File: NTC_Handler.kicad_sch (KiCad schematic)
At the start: 47 parts

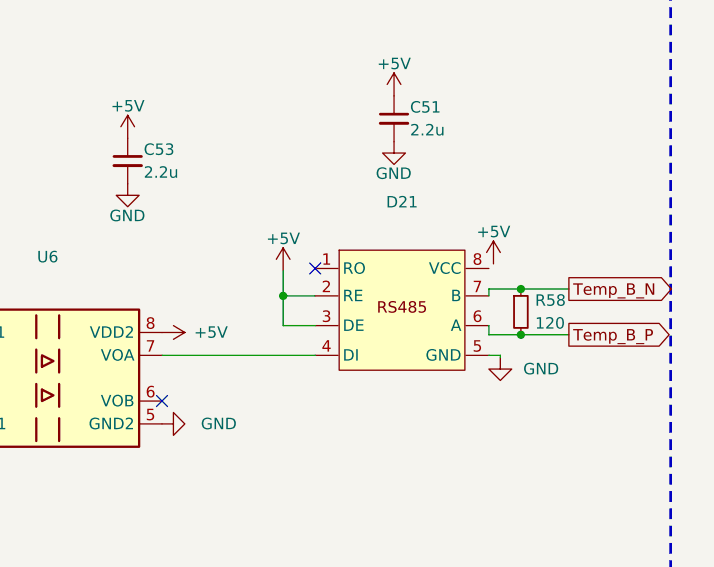
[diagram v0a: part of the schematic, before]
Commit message: VER2.2: доработал мелкие недостатки, оптимизировал дорожки и полигоны
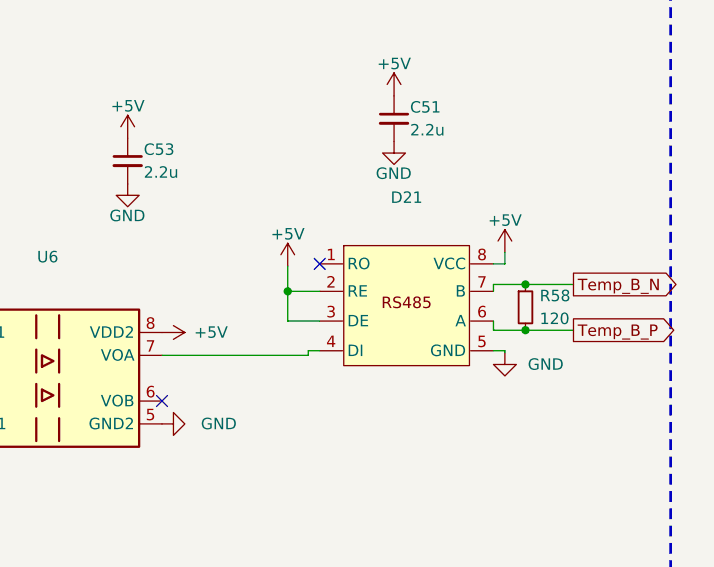
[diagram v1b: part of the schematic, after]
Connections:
- net +5V: now also D21.8 (VCC)
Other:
- moved on the sheet: D21, R58
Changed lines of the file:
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@@
 	)
 	(junction
-		(at 268.732 148.336)
+		(at 269.24 147.828)
 		(diameter 0)
 		(color 0 0 0 0)
@@
 	)
 	(junction
-		(at 295.148 147.574)
+		(at 295.656 147.066)
 		(diameter 0)
 		(color 0 0 0 0)
 	)
 	(junction
-		(at 295.148 152.654)
+		(at 295.656 152.146)
 		(diameter 0)
 		(color 0 0 0 0)
@@
 	)
 	(no_connect
-		(at 272.288 145.288)
+		(at 272.796 144.78)
 	)
 	(no_connect
@@
 	(wire
 		(pts
+			(xy 292.1 144.78) (xy 293.37 144.78)
+		)
+		(stroke
+			(width 0)
+			(type default)
+		)
+	)
+	(wire
+		(pts
 			(xy 174.625 152.4) (xy 174.625 156.21)
 		)
@@
 	(wire
 		(pts
-			(xy 291.592 147.574) (xy 291.592 148.336)
+			(xy 292.1 147.066) (xy 292.1 147.828)
 		)
 		(stroke
@@
 	(wire
 		(pts
-			(xy 268.732 148.336) (xy 268.732 151.638)
+			(xy 269.24 147.828) (xy 269.24 151.13)
 		)
 		(stroke
@@
 	(wire
 		(pts
-			(xy 255.27 154.94) (xy 272.288 154.94)
+			(xy 271.526 154.432) (xy 272.796 154.432)
 		)
 		(stroke
@@
 	(wire
 		(pts
-			(xy 268.732 151.638) (xy 272.288 151.638)
+			(xy 269.24 151.13) (xy 272.796 151.13)
 		)
 		(stroke
@@
 	(wire
 		(pts
-			(xy 295.148 147.574) (xy 291.592 147.574)
+			(xy 295.656 147.066) (xy 292.1 147.066)
 		)
 		(stroke
@@
 	(wire
 		(pts
-			(xy 292.862 154.94) (xy 292.862 155.194)
+			(xy 293.37 154.432) (xy 293.37 154.686)
 		)
 		(stroke
@@
 	(wire
 		(pts
-			(xy 295.148 152.654) (xy 300.482 152.654)
+			(xy 295.656 152.146) (xy 300.99 152.146)
 		)
 		(stroke
@@
 	(wire
 		(pts
+			(xy 271.526 154.432) (xy 271.526 154.94)
+		)
+		(stroke
+			(width 0)
+			(type default)
+		)
+	)
+	(wire
+		(pts
 			(xy 53.34 138.43) (xy 58.42 138.43)
 		)
@@
 	(wire
 		(pts
-			(xy 295.148 147.574) (xy 300.482 147.574)
+			(xy 295.656 147.066) (xy 300.99 147.066)
 		)
 		(stroke
@@
 	(wire
 		(pts
-			(xy 291.592 154.94) (xy 292.862 154.94)
+			(xy 292.1 154.432) (xy 293.37 154.432)
 		)
 		(stroke
@@
 	(wire
 		(pts
-			(xy 295.148 152.654) (xy 291.592 152.654)
+			(xy 295.656 152.146) (xy 292.1 152.146)
 		)
 		(stroke
@@
 	(wire
 		(pts
-			(xy 291.592 152.654) (xy 291.592 151.638)
+			(xy 292.1 152.146) (xy 292.1 151.13)
 		)
 		(stroke
@@
 	(wire
 		(pts
-			(xy 268.732 148.336) (xy 272.288 148.336)
+			(xy 269.24 147.828) (xy 272.796 147.828)
+		)
+		(stroke
+			(width 0)
+			(type default)
+		)
+	)
+	(wire
+		(pts
+			(xy 271.526 154.94) (xy 255.27 154.94)
 		)
 		(stroke
@@
 	(wire
 		(pts
+			(xy 293.37 144.78) (xy 293.37 143.51)
+		)
+		(stroke
+			(width 0)
+			(type default)
+		)
+	)
+	(wire
+		(pts
 			(xy 198.12 139.7) (xy 212.09 139.7)
 		)
@@
 	(wire
 		(pts
-			(xy 268.732 145.542) (xy 268.732 148.336)
+			(xy 269.24 145.034) (xy 269.24 147.828)
 		)
 		(stroke
@@
 	(global_label "Temp_B_P"
 		(shape output)
-		(at 300.482 152.654 0)
+		(at 300.99 152.146 0)
 		(fields_autoplaced yes)
 		(effects
@@
 		)
 		(property "Intersheetrefs" "${INTERSHEET_REFS}"
-			(at 312.8409 152.654 0)
+			(at 313.3489 152.146 0)
 			(effects
 				(font
@@
 	(global_label "Temp_B_N"
 		(shape output)
-		(at 300.482 147.574 0)
+		(at 300.99 147.066 0)
 		(fields_autoplaced yes)
 		(effects
@@
 		)
 		(property "Intersheetrefs" "${INTERSHEET_REFS}"
-			(at 312.9014 147.574 0)
+			(at 313.4094 147.066 0)
 			(effects
 				(font
@@
 	(symbol
 		(lib_id "power:GND")
-		(at 292.862 155.194 0)
+		(at 293.37 154.686 0)
 		(unit 1)
 		(exclude_from_sim no)
@@
 		(fields_autoplaced yes)
 		(property "Reference" "#PWR082"
-			(at 292.862 161.544 0)
+			(at 293.37 161.036 0)
 			(effects
 				(font
@@
 		)
 		(property "Value" "GND"
-			(at 295.402 156.4639 0)
+			(at 295.91 155.9559 0)
 			(effects
 				(font
@@
 		)
 		(property "Footprint" ""
-			(at 292.862 155.194 0)
+			(at 293.37 154.686 0)
 			(effects
 				(font
@@
 		)
 		(property "Datasheet" ""
-			(at 292.862 155.194 0)
+			(at 293.37 154.686 0)
 			(effects
 				(font
@@
 		)
 		(property "Description" "Power symbol creates a global label with name \"GND\" , ground"
-			(at 292.862 155.194 0)
+			(at 293.37 154.686 0)
 			(effects
 				(font
@@
 	(symbol
 		(lib_id "power:+5V")
-		(at 268.732 145.542 0)
+		(at 269.24 145.034 0)
 		(unit 1)
 		(exclude_from_sim no)
@@
 		(dnp no)
 		(property "Reference" "#PWR071"
-			(at 268.732 149.352 0)
+			(at 269.24 148.844 0)
 			(effects
 				(font
@@
 		)
 		(property "Value" "+5V"
-			(at 268.732 141.986 0)
+			(at 269.24 141.478 0)
 			(effects
 				(font
@@
 		)
 		(property "Footprint" ""
-			(at 268.732 145.542 0)
+			(at 269.24 145.034 0)
 			(effects
 				(font
@@
 		)
 		(property "Datasheet" ""
-			(at 268.732 145.542 0)
+			(at 269.24 145.034 0)
 			(effects
 				(font
@@
 		)
 		(property "Description" "Power symbol creates a global label with name \"+5V\""
-			(at 268.732 145.542 0)
+			(at 269.24 145.034 0)
 			(effects
 				(font
@@
 	(symbol
 		(lib_id "Interface_My:ADM3485E")
-		(at 281.94 140.716 0)
+		(at 282.448 140.208 0)
 		(unit 1)
 		(exclude_from_sim no)
@@
 		(fields_autoplaced yes)
 		(property "Reference" "D21"
-			(at 281.94 137.922 0)
+			(at 282.448 137.414 0)
 			(effects
 				(font
@@
 		)
 		(property "Value" "~"
-			(at 281.94 140.462 0)
+			(at 282.448 139.954 0)
 			(effects
 				(font
@@
 		)
 		(property "Footprint" "Package_SO:SOIC-8_3.9x4.9mm_P1.27mm"
-			(at 281.94 140.081 0)
+			(at 282.448 139.573 0)
 			(effects
 				(font
@@
 		)
 		(property "Datasheet" ""
-			(at 281.94 140.081 0)
+			(at 282.448 139.573 0)
 			(effects
 				(font
@@
 		)
 		(property "Description" ""
-			(at 281.94 140.716 0)
+			(at 282.448 140.208 0)
 			(effects
 				(font
@@
 		)
 		(property "Description P/N" "RS485"
-			(at 281.94 140.716 0)
+			(at 282.448 140.208 0)
 			(effects
 				(font
@@
 		)
 		(property "Product Name" "SN65HVD3082EDR"
-			(at 281.94 140.716 0)
+			(at 282.448 140.208 0)
 			(effects
 				(font
@@
 		)
 		(property "Purpose" ""
-			(at 281.94 140.716 0)
+			(at 282.448 140.208 0)
 			(effects
 				(font
@@
 		)
 		(property "Replacement" ""
-			(at 281.94 140.716 0)
+			(at 282.448 140.208 0)
 			(effects
 				(font
@@
 	(symbol
 		(lib_id "power:+5V")
-		(at 292.1 144.78 0)
+		(at 293.37 143.51 0)
 		(unit 1)
 		(exclude_from_sim no)
@@
 		(dnp no)
 		(property "Reference" "#PWR072"
-			(at 292.1 148.59 0)
+			(at 293.37 147.32 0)
 			(effects
 				(font
@@
 		)
 		(property "Value" "+5V"
-			(at 292.1 141.224 0)
+			(at 293.37 139.954 0)
 			(effects
 				(font
@@
 		)
 		(property "Footprint" ""
-			(at 292.1 144.78 0)
+			(at 293.37 143.51 0)
 			(effects
 				(font
@@
 		)
 		(property "Datasheet" ""
-			(at 292.1 144.78 0)
+			(at 293.37 143.51 0)
 			(effects
 				(font
@@
 		)
 		(property "Description" "Power symbol creates a global label with name \"+5V\""
-			(at 292.1 144.78 0)
+			(at 293.37 143.51 0)
 			(effects
 				(font
@@
 	(symbol
 		(lib_id "Device:R_Small")
-		(at 295.148 150.114 0)
+		(at 295.656 149.606 0)
 		(unit 1)
 		(exclude_from_sim no)
@@
 		(dnp no)
 		(property "Reference" "R58"
-			(at 296.7228 148.8439 0)
+			(at 297.2308 148.3359 0)
 			(effects
 				(font
@@
 		)
 		(property "Value" "120"
-			(at 296.7228 151.3839 0)
+			(at 297.2308 150.8759 0)
 			(effects
 				(font
@@
 		)
 		(property "Footprint" "Resistor_SMD:R_0805_2012Metric_Pad1.20x1.40mm_HandSolder"
-			(at 295.148 150.114 0)
+			(at 295.656 149.606 0)
 			(effects
 				(font
@@
 		)
 		(property "Datasheet" "~"
-			(at 295.148 150.114 0)
+			(at 295.656 149.606 0)
 			(effects
 				(font
@@
 		)
 		(property "Description" "Resistor, small symbol"
-			(at 295.148 150.114 0)
+			(at 295.656 149.606 0)
 			(effects
 				(font
@@
 		)
 		(property "Description P/N" ""
-			(at 295.148 150.114 0)
+			(at 295.656 149.606 0)
 			(effects
 				(font
@@
 		)
 		(property "Product Name" ""
-			(at 295.148 150.114 0)
+			(at 295.656 149.606 0)
 			(effects
 				(font
@@
 		)
 		(property "Purpose" ""
-			(at 295.148 150.114 0)
+			(at 295.656 149.606 0)
 			(effects
 				(font
@@
 		)
 		(property "Replacement" ""
-			(at 295.148 150.114 0)
+			(at 295.656 149.606 0)
 			(effects
 				(font

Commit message: VER2.2: обновил BOM, добавил лист закупки
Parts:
- D52: Description P/N (none) -> DCDC; Product Name (none) -> B1505LS-1WR3
- L25: Description P/N (none) -> Inductor SMD; Product Name (none) -> MLZ2012M6R8WT000
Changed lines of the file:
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@@
 				)
 				(justify left)
+				(hide yes)
 			)
 		)
@@
 			)
 		)
+		(property "Description P/N" "DCDC"
+			(at 81.28 147.32 0)
+			(effects
+				(font
+					(size 1.27 1.27)
+				)
+				(hide yes)
+			)
+		)
+		(property "Product Name" "B1505LS-1WR3  "
+			(at 81.28 147.32 0)
+			(effects
+				(font
+					(size 1.27 1.27)
+				)
+				(hide yes)
+			)
+		)
 		(pin "1"
 		)
@@
 			(effects
 				(font
+					(size 1.27 1.27)
+				)
+				(hide yes)
+			)
+		)
+		(property "Description P/N" "Inductor SMD"
+			(at 63.5 138.43 90)
+			(effects
+				(font
+					(size 1.27 1.27)
+				)
+				(hide yes)
+			)
+		)
+		(property "Product Name" "MLZ2012M6R8WT000 "
+			(at 63.5 138.43 90)
+			(effects
+				(font

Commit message: VER2.2.1: исправил косяк с питанием NTC, изменил номиналы затворов и цепи NTC
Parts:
- C29, C56, C81: value 10n -> 1n
- R25, R26, R57, R59, R64, R70: value 30k -> 10k
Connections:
- net +5VA: now also C102.2, D52.6 (+Vo); no longer C102.1, D52.4 (0V)
- net GNDA: now also C102.1, D52.4 (0V); no longer C102.2, D52.6 (+Vo)
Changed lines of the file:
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@@
 	(symbol
 		(lib_id "power:+5VA")
-		(at 66.04 146.05 90)
+		(at 66.04 151.13 90)
 		(unit 1)
 		(exclude_from_sim no)
@@
 		(fields_autoplaced yes)
 		(property "Reference" "#PWR0126"
-			(at 69.85 146.05 0)
+			(at 69.85 151.13 0)
 			(effects
 				(font
@@
 		)
 		(property "Value" "+5VA"
-			(at 62.23 146.05 90)
+			(at 62.23 151.13 90)
 			(effects
 				(font
@@
 		)
 		(property "Footprint" ""
-			(at 66.04 146.05 0)
+			(at 66.04 151.13 0)
 			(effects
 				(font
@@
 		)
 		(property "Datasheet" ""
-			(at 66.04 146.05 0)
+			(at 66.04 151.13 0)
 			(effects
 				(font
@@
 		)
 		(property "Description" "Power symbol creates a global label with name \"+5VA\""
-			(at 66.04 146.05 0)
+			(at 66.04 151.13 0)
 			(effects
 				(font
@@
 			)
 		)
-		(property "Value" "10n"
+		(property "Value" "1n"
 			(at 184.023 172.72 0)
 			(effects
@@
 	(symbol
 		(lib_id "power:GNDA")
-		(at 66.04 151.13 270)
+		(at 66.04 146.05 270)
 		(unit 1)
 		(exclude_from_sim no)
@@
 		(fields_autoplaced yes)
 		(property "Reference" "#PWR0125"
-			(at 59.69 151.13 0)
+			(at 59.69 146.05 0)
 			(effects
 				(font
@@
 		)
 		(property "Value" "GNDA"
-			(at 62.23 151.13 90)
+			(at 62.23 146.05 90)
 			(effects
 				(font
@@
 		)
 		(property "Footprint" ""
-			(at 66.04 151.13 0)
+			(at 66.04 146.05 0)
 			(effects
 				(font
@@
 		)
 		(property "Datasheet" ""
-			(at 66.04 151.13 0)
+			(at 66.04 146.05 0)
 			(effects
 				(font
@@
 		)
 		(property "Description" "Power symbol creates a global label with name \"GNDA\" , analog ground"
-			(at 66.04 151.13 0)
+			(at 66.04 146.05 0)
 			(effects
 				(font
@@
 			)
 		)
-		(property "Value" "30k"
+		(property "Value" "10k"
 			(at 174.625 158.75 90)
 			(effects
@@
 			)
 		)
-		(property "Value" "30k"
+		(property "Value" "10k"
 			(at 173.99 223.52 90)
 			(effects
@@
 			)
 		)
-		(property "Value" "30k"
+		(property "Value" "10k"
 			(at 175.26 69.85 90)
 			(effects
@@
 			)
 		)
-		(property "Value" "30k"
+		(property "Value" "10k"
 			(at 174.625 147.32 90)
 			(effects
@@
 			)
 		)
-		(property "Value" "10n"
+		(property "Value" "1n"
 			(at 184.658 97.79 0)
 			(effects
@@
 			)
 		)
-		(property "Value" "30k"
+		(property "Value" "10k"
 			(at 175.26 81.28 90)
 			(effects
@@
 			)
 		)
-		(property "Value" "30k"
+		(property "Value" "10k"
 			(at 173.99 236.22 90)
 			(effects
@@
 			)
 		)
-		(property "Value" "10n"
+		(property "Value" "1n"
 			(at 185.928 251.46 0)
 			(effects

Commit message: VER2.2.1: создал папку для производственных доков
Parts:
- C102, C28, C29, C30, C40, C41, C42, C50, C51, C52, C53, C54, C55, C56, C75, C76, C77, C78, C79, C80, C81: Description P/N (none) -> Capacitor SMD 25+V
- R25, R26, R27, R28, R29, R56, R57, R58, R59, R60, R63, R64, R65, R70, R72: Description P/N (none) -> Resistor SMD
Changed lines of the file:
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@@
 			)
 		)
-		(property "Description P/N" ""
+		(property "Description P/N" "Resistor SMD"
 			(at 195.58 134.62 0)
 			(effects
@@
 			)
 		)
-		(property "Description P/N" ""
+		(property "Description P/N" "Capacitor SMD 25+V"
 			(at 281.051 128.651 0)
 			(effects
@@
 			)
 		)
-		(property "Description P/N" ""
+		(property "Description P/N" "Capacitor SMD 25+V"
 			(at 68.58 140.97 0)
 			(effects
@@
 			)
 		)
-		(property "Description P/N" ""
+		(property "Description P/N" "Capacitor SMD 25+V"
 			(at 195.58 139.7 0)
 			(effects
@@
 			)
 		)
-		(property "Description P/N" ""
+		(property "Description P/N" "Capacitor SMD 25+V"
 			(at 232.41 57.15 0)
 			(effects
@@
 			)
 		)
-		(property "Description P/N" ""
+		(property "Description P/N" "Capacitor SMD 25+V"
 			(at 182.245 171.45 0)
 			(effects
@@
 			)
 		)
-		(property "Description P/N" ""
+		(property "Description P/N" "Resistor SMD"
 			(at 174.625 158.75 0)
 			(effects
@@
 			)
 		)
-		(property "Description P/N" ""
+		(property "Description P/N" "Capacitor SMD 25+V"
 			(at 191.135 123.19 0)
 			(effects
@@
 			)
 		)
-		(property "Description P/N" ""
+		(property "Description P/N" "Resistor SMD"
 			(at 173.99 223.52 0)
 			(effects
@@
 			)
 		)
-		(property "Description P/N" ""
+		(property "Description P/N" "Capacitor SMD 25+V"
 			(at 252.095 57.785 0)
 			(effects
@@
 			)
 		)
-		(property "Description P/N" ""
+		(property "Description P/N" "Resistor SMD"
 			(at 175.26 69.85 0)
 			(effects
@@
 			)
 		)
-		(property "Description P/N" ""
+		(property "Description P/N" "Resistor SMD"
 			(at 174.625 147.32 0)
 			(effects
@@
 			)
 		)
-		(property "Description P/N" ""
+		(property "Description P/N" "Capacitor SMD 25+V"
 			(at 195.58 63.5 0)
 			(effects
@@
 			)
 		)
-		(property "Description P/N" ""
+		(property "Description P/N" "Resistor SMD"
 			(at 212.09 85.09 0)
 			(effects
@@
 			)
 		)
-		(property "Description P/N" ""
+		(property "Description P/N" "Capacitor SMD 25+V"
 			(at 182.88 96.52 0)
 			(effects
@@
 			)
 		)
-		(property "Description P/N" ""
+		(property "Description P/N" "Resistor SMD"
 			(at 294.767 74.041 0)
 			(effects
@@
 			)
 		)
-		(property "Description P/N" ""
+		(property "Description P/N" "Capacitor SMD 25+V"
 			(at 252.095 210.185 0)
 			(effects
@@
 			)
 		)
-		(property "Description P/N" ""
+		(property "Description P/N" "Resistor SMD"
 			(at 175.26 81.28 0)
 			(effects
@@
 			)
 		)
-		(property "Description P/N" ""
+		(property "Description P/N" "Resistor SMD"
 			(at 173.99 236.22 0)
 			(effects
@@
 			)
 		)
-		(property "Description P/N" ""
+		(property "Description P/N" "Resistor SMD"
 			(at 212.09 160.655 0)
 			(effects
@@
 			)
 		)
-		(property "Description P/N" ""
+		(property "Description P/N" "Capacitor SMD 25+V"
 			(at 58.42 140.97 0)
 			(effects
@@
 			)
 		)
-		(property "Description P/N" ""
+		(property "Description P/N" "Capacitor SMD 25+V"
 			(at 229.87 133.35 0)
 			(effects
@@
 			)
 		)
-		(property "Description P/N" ""
+		(property "Description P/N" "Resistor SMD"
 			(at 195.58 58.42 0)
 			(effects
@@
 			)
 		)
-		(property "Description P/N" ""
+		(property "Description P/N" "Capacitor SMD 25+V"
 			(at 251.46 133.35 0)
 			(effects
@@
 			)
 		)
-		(property "Description P/N" ""
+		(property "Description P/N" "Resistor SMD"
 			(at 294.767 226.441 0)
 			(effects
@@
 			)
 		)
-		(property "Description P/N" ""
+		(property "Description P/N" "Capacitor SMD 25+V"
 			(at 281.051 52.451 0)
 			(effects
@@
 			)
 		)
-		(property "Description P/N" ""
+		(property "Description P/N" "Capacitor SMD 25+V"
 			(at 193.04 46.99 0)
 			(effects
@@
 			)
 		)
-		(property "Description P/N" ""
+		(property "Description P/N" "Capacitor SMD 25+V"
 			(at 193.04 199.39 0)
 			(effects
@@
 			)
 		)
-		(property "Description P/N" ""
+		(property "Description P/N" "Resistor SMD"
 			(at 195.58 213.36 0)
 			(effects
@@
 			)
 		)
-		(property "Description P/N" ""
+		(property "Description P/N" "Resistor SMD"
 			(at 212.09 238.76 0)
 			(effects
@@
 			)
 		)
-		(property "Description P/N" ""
+		(property "Description P/N" "Capacitor SMD 25+V"
 			(at 68.58 148.59 0)
 			(effects
@@
 			)
 		)
-		(property "Description P/N" ""
+		(property "Description P/N" "Capacitor SMD 25+V"
 			(at 195.58 218.44 0)
 			(effects
@@
 			)
 		)
-		(property "Description P/N" ""
+		(property "Description P/N" "Capacitor SMD 25+V"
 			(at 281.051 204.851 0)
 			(effects
@@
 			)
 		)
-		(property "Description P/N" ""
+		(property "Description P/N" "Capacitor SMD 25+V"
 			(at 184.15 250.19 0)
 			(effects
@@
 			)
 		)
-		(property "Description P/N" ""
+		(property "Description P/N" "Resistor SMD"
 			(at 295.656 149.606 0)
 			(effects
@@
 			)
 		)
-		(property "Description P/N" ""
+		(property "Description P/N" "Capacitor SMD 25+V"
 			(at 231.14 210.82 0)
 			(effects

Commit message: VER2.2.1: исправил все доки
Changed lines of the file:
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@@
 		(date "2025-06-04")
 		(company "ООО \"ЭТТ\"")
+		(comment 1 "НВЦТ.EVP150-2-1.2000.120_v1 Э3")
 	)
 	(rectangle
@@
 					(size 1.27 1.27)
 				)
+				(hide yes)
 			)
 		)
@@
 					(size 1.27 1.27)
 				)
+				(hide yes)
 			)
 		)
@@
 					(size 1.27 1.27)
 				)
+				(hide yes)
 			)
 		)
@@
 					(size 1.27 1.27)
 				)
+				(hide yes)
 			)
 		)
@@
 					(size 1.27 1.27)
 				)
+				(hide yes)
 			)
 		)
@@
 					(size 1.27 1.27)
 				)
+				(hide yes)
 			)
 		)
@@
 					(size 1.27 1.27)
 				)
+				(hide yes)
 			)
 		)
@@
 					(size 1.27 1.27)
 				)
+				(hide yes)
 			)
 		)
@@
 					(size 1.27 1.27)
 				)
+				(hide yes)
 			)
 		)
@@
 					(size 1.27 1.27)
 				)
+				(hide yes)
 			)
 		)
@@
 					(size 1.27 1.27)
 				)
+				(hide yes)
 			)
 		)
@@
 					(size 1.27 1.27)
 				)
+				(hide yes)
 			)
 		)
@@
 					(size 1.27 1.27)
 				)
+				(hide yes)
 			)
 		)
@@
 					(size 1.27 1.27)
 				)
+				(hide yes)
 			)
 		)
@@
 					(size 1.27 1.27)
 				)
+				(hide yes)
 			)
 		)
@@
 					(size 1.27 1.27)
 				)
+				(hide yes)
 			)
 		)
@@
 					(size 1.27 1.27)
 				)
+				(hide yes)
 			)
 		)
@@
 					(size 1.27 1.27)
 				)
+				(hide yes)
 			)
 		)
@@
 					(size 1.27 1.27)
 				)
+				(hide yes)
 			)
 		)
@@
 					(size 1.27 1.27)
 				)
+				(hide yes)
 			)
 		)
@@
 					(size 1.27 1.27)
 				)
+				(hide yes)
 			)
 		)
@@
 					(size 1.27 1.27)
 				)
+				(hide yes)
 			)
 		)
@@
 					(size 1.27 1.27)
 				)
+				(hide yes)
 			)
 		)
@@
 					(size 1.27 1.27)
 				)
+				(hide yes)
 			)
 		)
@@
 					(size 1.27 1.27)
 				)
+				(hide yes)
 			)
 		)
@@
 					(size 1.27 1.27)
 				)
+				(hide yes)
 			)
 		)
@@
 					(size 1.27 1.27)
 				)
+				(hide yes)
 			)
 		)
@@
 					(size 1.27 1.27)
 				)
+				(hide yes)
 			)
 		)
@@
 					(size 1.27 1.27)
 				)
+				(hide yes)
 			)
 		)
@@
 					(size 1.27 1.27)
 				)
+				(hide yes)
 			)
 		)
@@
 					(size 1.27 1.27)
 				)
+				(hide yes)
 			)
 		)
@@
 					(size 1.27 1.27)
 				)
+				(hide yes)
 			)
 		)
@@
 					(size 1.27 1.27)
 				)
+				(hide yes)
 			)
 		)
@@
 					(size 1.27 1.27)
 				)
+				(hide yes)
 			)
 		)
@@
 					(size 1.27 1.27)
 				)
+				(hide yes)
 			)
 		)
